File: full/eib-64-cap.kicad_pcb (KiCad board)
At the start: 2 copper layers, 140.4 x 111.2 mm, 48 parts, among them J1 DF40C-70DP-0.4V(51), J10 DF40C-70DP-0.4V(51), J11 DF40C-70DP-0.4V(51), J12 DF40C-70DP-0.4V(51), J2 DF40C-70DP-0.4V(51), J3 DF40C-70DP-0.4V(51), J4 DF40C-70DP-0.4V(51), J5 DF40C-70DP-0.4V(51), J6 DF40C-70DP-0.4V(51), J7 DF40C-70DP-0.4V(51)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

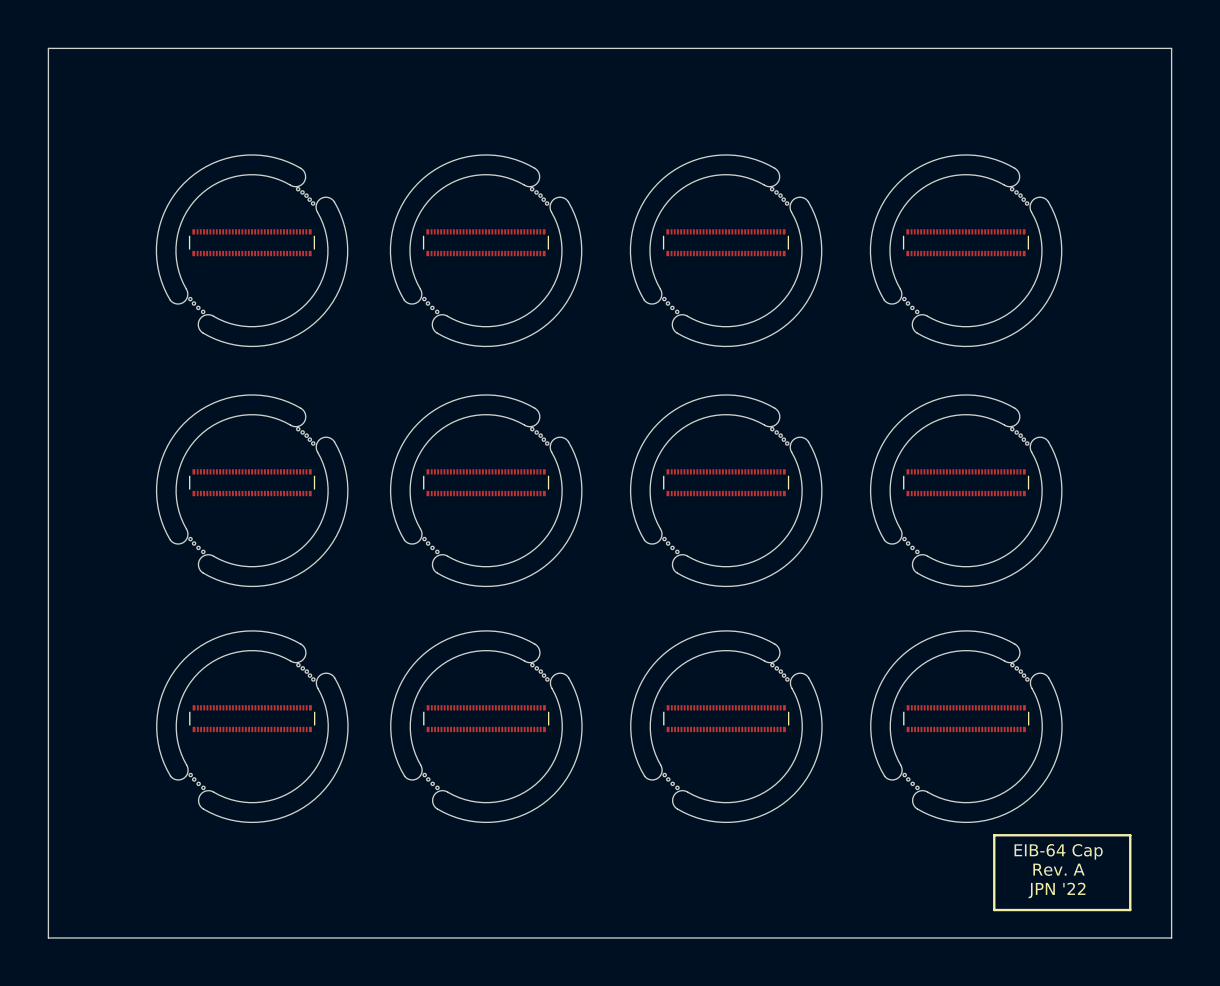
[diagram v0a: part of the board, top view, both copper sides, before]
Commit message: Add hats to EIB cap with ferrule
- Remove copper from mouse bites to prevent burs
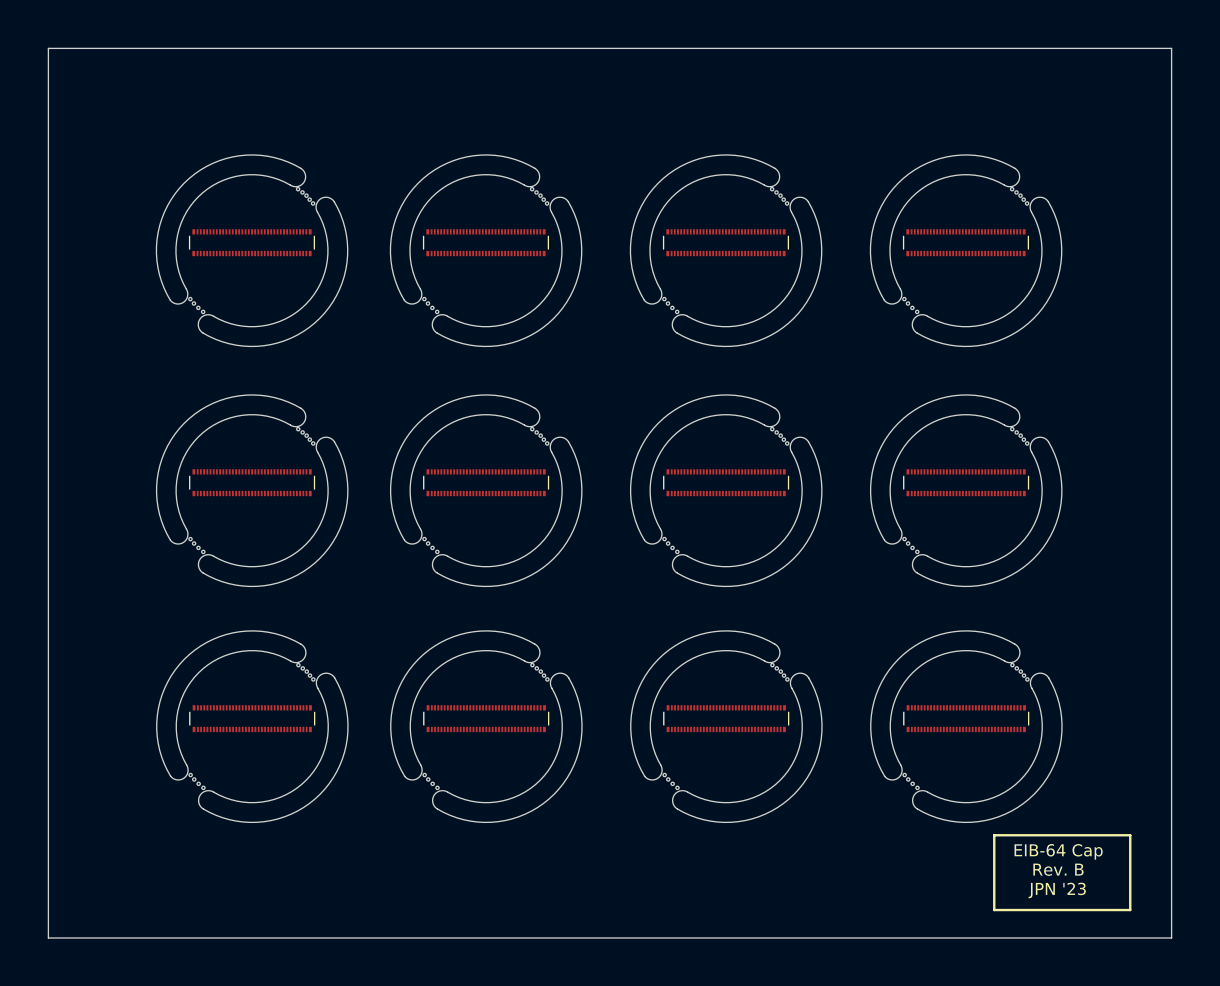
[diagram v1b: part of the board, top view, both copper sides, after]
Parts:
- removed the G*** at (111.5, 93.3)
- removed the G*** at (82.3, 93.3)
- removed the G*** at (82.3, 123.0)
- removed the G*** at (171.6, 63.6)
- removed the G*** at (82.2, 63.6)
- removed the G*** at (141.5, 63.4)
- removed the G*** at (111.5, 123.0)
- removed the G*** at (171.5, 122.9)
- removed the G*** at (171.5, 93.3)
- removed the G*** at (142.0, 122.9)
- removed the G*** at (111.5, 63.6)
- removed the G*** at (141.5, 93.3)
- added G***: LOGO, LOGO, F.Cu at (142.2, 92.8)
- added G***: LOGO, LOGO, F.Cu at (82.6, 62.9)
- added G***: LOGO, LOGO, F.Cu at (172.0, 92.8)
- added G***: LOGO, LOGO, F.Cu at (172.0, 122.4)
- added G***: LOGO, LOGO, F.Cu at (112.4, 122.4)
- added G***: LOGO, LOGO, F.Cu at (112.4, 92.8)
- added G***: LOGO, LOGO, F.Cu at (82.6, 122.4)
- added G***: LOGO, LOGO, F.Cu at (142.2, 122.4)
- added G***: LOGO, LOGO, F.Cu at (142.2, 62.9)
- added G***: LOGO, LOGO, F.Cu at (172.0, 62.9)
- added G***: LOGO, LOGO, F.Cu at (112.4, 62.9)
- added G***: LOGO, LOGO, F.Cu at (82.6, 92.8)
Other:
- board text added: "EIB-64 Cap Rev. B JPN '23"
- board text removed: "EIB-64 Cap Rev. A JPN '22"

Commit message: Updated caps.
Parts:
- removed the G*** at (142.2, 92.8)
- removed the G*** at (82.6, 62.9)
- removed the G*** at (172.0, 92.8)
- removed the G*** at (172.0, 122.4)
- removed the G*** at (112.4, 122.4)
- removed the G*** at (112.4, 92.8)
- removed the G*** at (82.6, 122.4)
- removed the G*** at (142.2, 122.4)
- removed the G*** at (142.2, 62.9)
- removed the G*** at (172.0, 62.9)
- removed the G*** at (112.4, 62.9)
- removed the G*** at (82.6, 92.8)
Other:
- board text added: "EIB-64 Cap Rev. C JPN '25"
- board text added: "open-ephys.org"
- board text removed: "EIB-64 Cap Rev. B JPN '23"
